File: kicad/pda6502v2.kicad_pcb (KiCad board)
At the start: 4 copper layers, 100 x 100 mm, 91 parts, among them J1 GPIO1, J2 GPIO2, J3 UART, J4 Screw_Terminal_01x02, J5 Conn_02x04_Odd_Even, J6 ICSP, J7 SPI, J8 FPGA_EXT, J9 SID, SW1 SW_Push, SW2 SW_Push, U1 W65C02SxP, U10 LT3030, U11 SC28L92A1B, U2 W65C22SxP, U3 W65C22SxP, U4 DS1818, U5 AS6C4008-55PCN, U6 ARMSID, U7 AT25M01, U8 ICE40HX4K-TQ144, U9 TLV1117-33, X1 8 MHz, X2 3.6864 MHz

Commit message: routing WIP: mostly ICSP to flash, a bit of BLINKEN
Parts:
- moved C10 25.2 mm to (132.9, 122.9)
- moved U7 19.3 mm to (131.6, 122.2)
- moved X1 5.36 mm to (132.1, 115.1)
- moved D11 5.06 mm to (102.9, 121.4), turned to 180 degrees
- moved U6 2.84 mm to (110.5, 90.2)
- moved C31 2.84 mm to (121.9, 102.9)
- moved C28 2.84 mm to (121.9, 100.3)
- moved C9 2.84 mm to (122.7, 90.2)
- moved J5 2.54 mm to (101.6, 110.5)
- moved SW2 2.54 mm to (101.6, 105.4)
- moved C2 1.27 mm to (154.9, 92.7)
- moved C6 1.27 mm to (174.0, 92.7)
- moved C1 1.27 mm to (135.9, 62.2)
- moved C4 1.27 mm to (124.5, 44.5)
- moved U1 1.27 mm to (132.1, 44.5)
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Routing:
- net /FLASH_~CS: track 0.00 -> 42.3 mm
- net /FLASH_SCK: track 0.00 -> 38.6 mm
- net /VCC_FLASH: track 0.00 -> 38.6 mm, vias 0 -> 3
- net /FLASH_MISO: track 0.00 -> 33.4 mm
- net /FLASH_MOSI: track 0.00 -> 31.5 mm
- net +2V5: track 125.9 -> 100.1 mm
- net /~RESET: track 21.5 -> 14.8 mm
- net +3V3: track 61.5 -> 68.2 mm
- net +5V: track 90.8 -> 84.6 mm
- net +1V2: track 97.1 -> 91.1 mm
- net GND: track 70.7 -> 65.7 mm, vias 21 -> 22
- net /UART_RXB~IRQ: track 14.0 -> 12.3 mm
- net /CLOCKSRC: track 7.79 -> 8.69 mm
- net Net-(U11-Pad30): track 20.9 -> 21.7 mm
- net /SPI_CLOCK: track 35.0 -> 34.3 mm
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
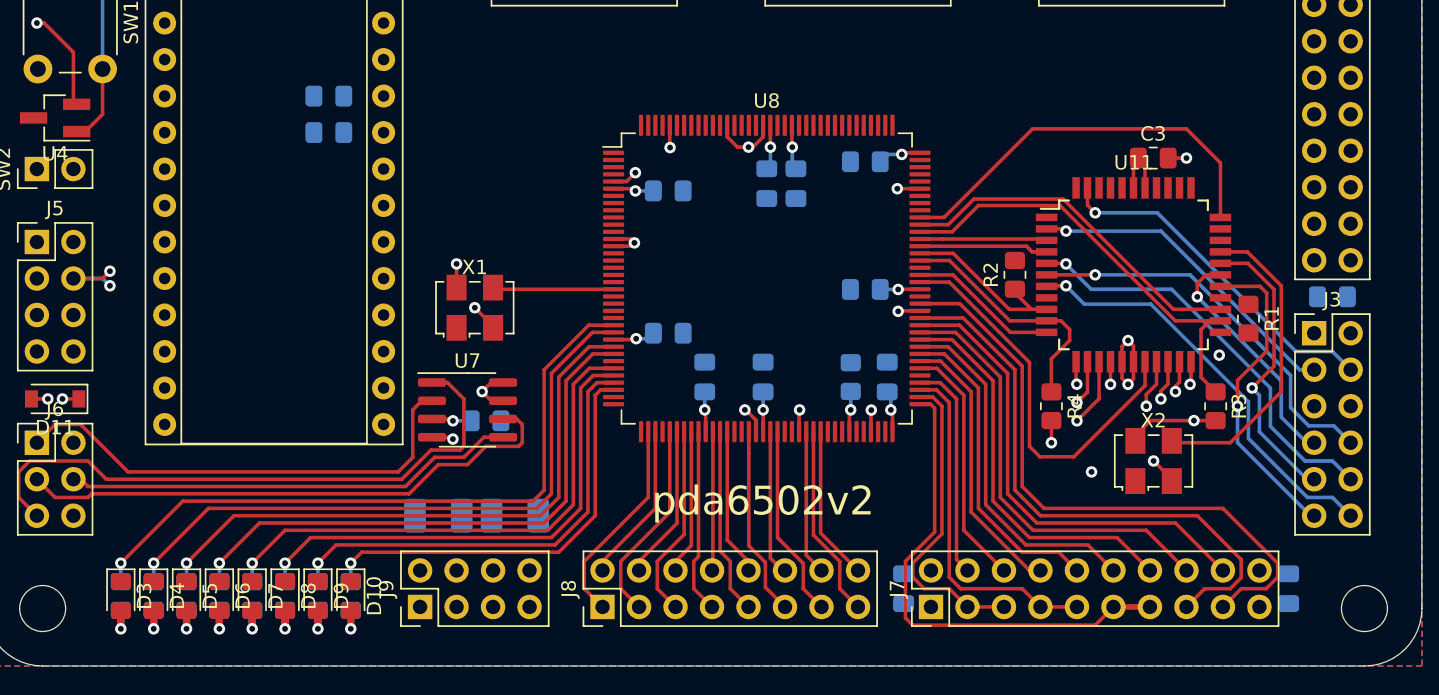
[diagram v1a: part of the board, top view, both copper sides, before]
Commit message: routing/placement; SID, FPGA, UART shifted away from centre.
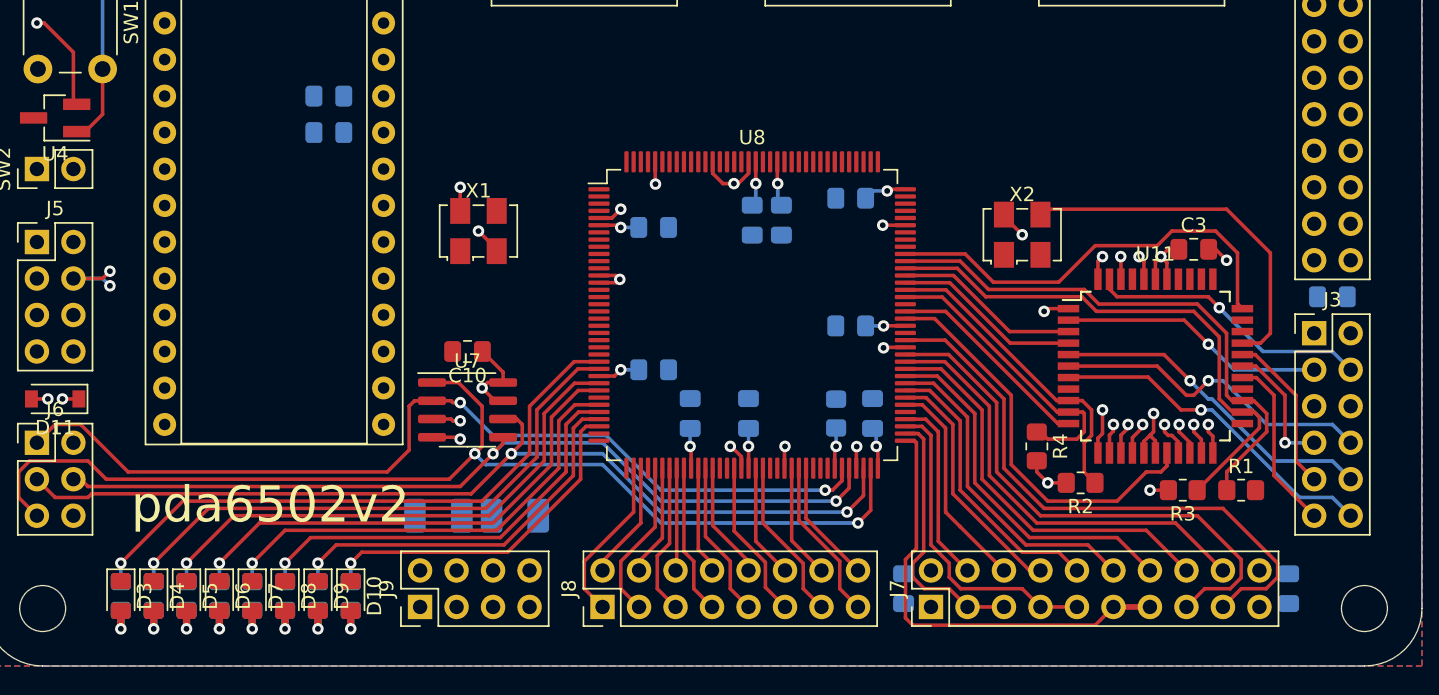
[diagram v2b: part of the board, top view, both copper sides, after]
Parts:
- C10: moved to F.Cu
- moved X2 18.2 mm to (170.2, 110.0)
- moved R2 15.2 mm to (174.2, 127.3), turned to 180 degrees
- moved R1 11.9 mm to (185.4, 127.8), turned to 0 degrees
- moved C3 6.95 mm to (182.1, 111.0)
- moved U11 6.53 mm to (179.5, 119.1)
- moved R3 6.27 mm to (181.4, 127.8), turned to 180 degrees
- moved X1 5.34 mm to (132.3, 109.7)
- moved C10 5.00 mm to (131.6, 118.1), turned to 180 degrees
- moved R4 2.97 mm to (171.2, 124.7)
- moved C22 2.74 mm to (144.5, 109.5)
- moved C14 2.74 mm to (158.2, 116.3)
- moved C17 2.74 mm to (159.8, 122.4)
- moved C23 2.74 mm to (151.4, 109.0)
- moved C24 2.74 mm to (158.2, 107.4)
- moved U8 2.74 mm to (151.4, 115.6)
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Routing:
- net /FLASH_~CS: track 42.3 -> 77.4 mm, vias 0 -> 2
- net +1V2: track 91.1 -> 124.8 mm
- net /FLASH_MISO: track 33.4 -> 65.5 mm, vias 0 -> 2
- net /FLASH_MOSI: track 31.5 -> 60.3 mm, vias 0 -> 2
- net /FLASH_SCK: track 38.6 -> 67.2 mm, vias 0 -> 2
- net +2V5: track 100.1 -> 125.9 mm
- net +5V: track 84.6 -> 99.0 mm
- net /UART_RXA~IRQ: track 24.8 -> 38.6 mm
- net /UARTA_RTS: track 22.4 -> 12.5 mm, vias 1 -> 0
- net /UART_RXB~IRQ: track 12.3 -> 22.0 mm
- net /UARTA_RX: track 20.4 -> 11.8 mm, vias 1 -> 0
- net /CLOCKSRC: track 8.69 -> 0.42 mm
- net /UART_TXA~IRQ: track 30.6 -> 37.6 mm
- net /UARTA_TX: track 16.6 -> 10.2 mm
- net /UARTB_RX: track 29.0 -> 23.2 mm
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
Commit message: more routing; SID connector, misc power etc.
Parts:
- moved C8 5.98 mm to (193.8, 81.3), turned to 0 degrees
- moved C7 2.03 mm to (189.7, 81.3)
- moved C5 0.82 mm to (190.8, 48.0), turned to 180 degrees
- moved C28 0.76 mm to (122.7, 100.3)
- moved C31 0.76 mm to (122.7, 102.9)
- moved C26 0.46 mm to (161.5, 134.9)
- moved C27 0.36 mm to (189.0, 134.4)
- turned C25 to 180 degrees
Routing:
- net +5V: track 99.0 -> 165.1 mm
- net /SID_X: track 0.00 -> 46.9 mm
- net /SID_Y: track 0.00 -> 42.8 mm
- net Net-(C29-Pad1): track 0.00 -> 42.4 mm
- net Net-(C30-Pad1): track 0.00 -> 40.4 mm
- net +3V3: track 67.0 -> 85.4 mm, vias 17 -> 20
- net +1V2: track 124.8 -> 132.4 mm, vias 4 -> 5
- net /SID_IN: track 0.00 -> 7.36 mm
- net GND: track 62.2 -> 69.2 mm, vias 18 -> 21
- net /SID_OUT: track 0.00 -> 3.96 mm
- net /VCC_FLASH: track 41.5 -> 44.9 mm

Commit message: Lots of routing. Nearly done, but getting tight.
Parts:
- removed the U3 at (170.2, 44.5)
- added U2: W65C22SxP, Package_DIP:DIP-40_W15.24mm, F.Cu at (151.1, 44.5)
- C28, C31: moved to F.Cu
- moved U3 19.1 mm to (170.2, 44.5)
- moved X2 9.56 mm to (179.3, 107.2)
- moved C10 7.89 mm to (129.5, 125.7)
- moved X1 7.27 mm to (135.4, 116.3)
- moved C31 6.60 mm to (129.3, 102.9), turned to 0 degrees
- moved C28 6.58 mm to (129.3, 100.3), turned to 0 degrees
- moved C29 6.48 mm to (136.0, 129.3), turned to 270 degrees
- moved C9 5.85 mm to (128.4, 91.4), turned to 270 degrees
- moved C2 4.88 mm to (151.1, 95.8), turned to 270 degrees
- moved C17 4.66 mm to (162.1, 126.5), turned to 0 degrees
- moved C15 4.26 mm to (145.8, 126.5), turned to 180 degrees
- moved C32 4.26 mm to (149.9, 126.5), turned to 180 degrees
- moved C22 4.20 mm to (140.7, 111.3), turned to 270 degrees
- moved R23 4.19 mm to (158.2, 126.5), turned to 0 degrees
- moved C30 2.30 mm to (132.6, 129.3), turned to 270 degrees
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- renumbered U2 to U3
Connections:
- J9 pad 3: /SID_X -> /SID_Y
- J9 pad 4: /SID_OUT -> /SID_X
- J9 pad 5: /SID_IN -> /SID_OUT
- J9 pad 6: /SID_Y -> /SID_IN
- U5 pad 10: /A2 -> /A5
- U5 pad 11: /A1 -> /A6
- U5 pad 12: /A0 -> /A7
- U5 pad 17: /D3 -> /D7
- U5 pad 18: /D4 -> /D6
- U5 pad 20: /D6 -> /D4
- U5 pad 21: /D7 -> /D3
- U5 pad 5: /A7 -> /A0
- U5 pad 6: /A6 -> /A1
- U5 pad 7: /A5 -> /A2
- U5 pad 8: /A4 -> /A3
- U5 pad 9: /A3 -> /A4
- U8 pad 12: Net-(U8-Pad12) -> /SID_~CS
- U8 pad 16: Net-(U8-Pad16) -> /RESET
- U8 pad 17: Net-(U8-Pad17) -> /~RESET
- U8 pad 22: /RESET -> Net-(U8-Pad22)
- U8 pad 23: /~RESET -> Net-(U8-Pad23)
- U8 pad 24: /SID_~CS -> Net-(U8-Pad24)
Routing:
- net /A3: track 1.78 -> 197.4 mm, vias 1 -> 7
- net /A2: track 1.70 -> 196.6 mm, vias 1 -> 7
- net /A1: track 1.58 -> 195.8 mm, vias 1 -> 7
- net /D0: track 2.12 -> 195.7 mm, vias 1 -> 5
- net /A0: track 1.71 -> 193.9 mm, vias 1 -> 7
- net /D1: track 3.13 -> 186.5 mm, vias 1 -> 5
- net /D2: track 2.21 -> 185.3 mm, vias 1 -> 5
- net /R~W: track 0.00 -> 164.6 mm, vias 0 -> 3
- net /D3: track 2.10 -> 166.1 mm, vias 1 -> 4
- net /D4: track 2.30 -> 164.0 mm, vias 1 -> 4
- net /D5: track 2.19 -> 154.1 mm, vias 1 -> 4
- net /D6: track 2.53 -> 151.3 mm, vias 1 -> 4
- net /D7: track 2.28 -> 142.1 mm, vias 1 -> 4
- net /CLOCK: track 0.00 -> 132.7 mm, vias 0 -> 3
- net /GPIO2A0: track 0.00 -> 94.5 mm, vias 0 -> 2
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
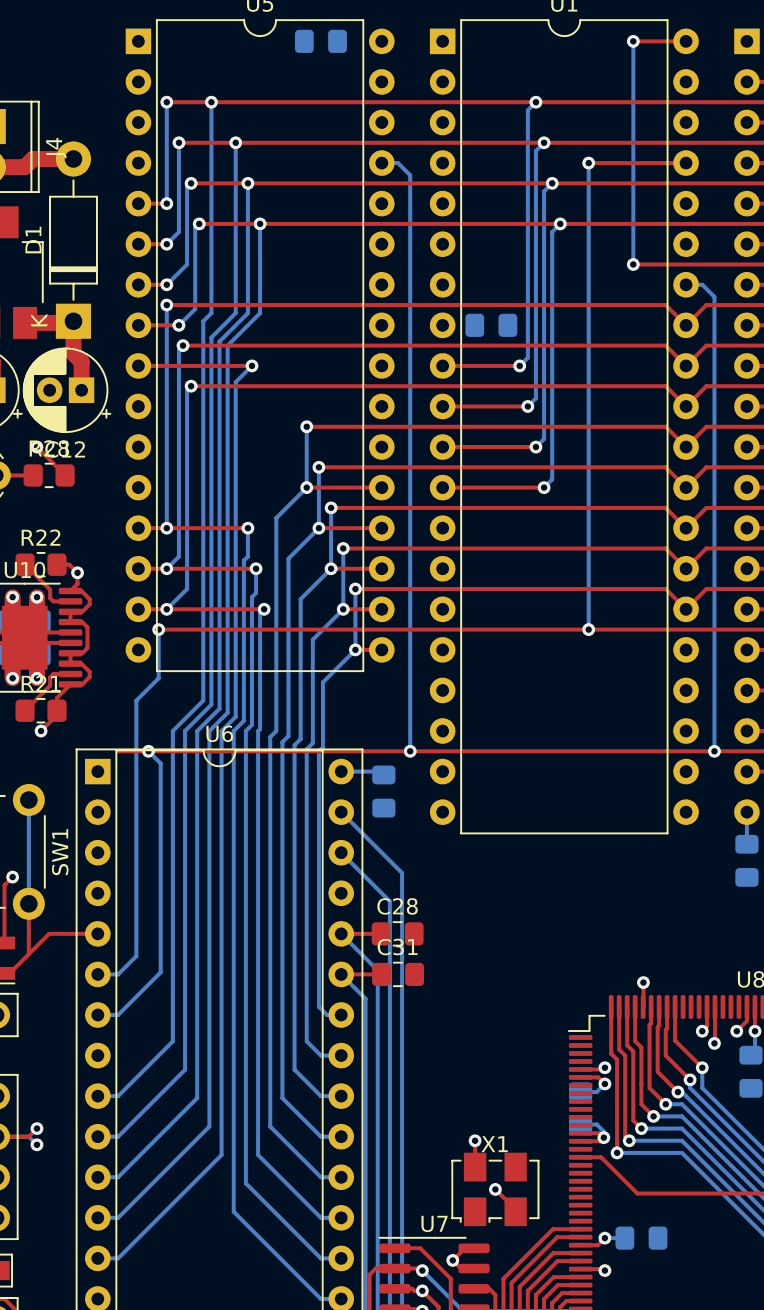
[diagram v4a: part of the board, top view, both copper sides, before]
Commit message: ARMSID routing improvements; fewer vias, straighter tracks.
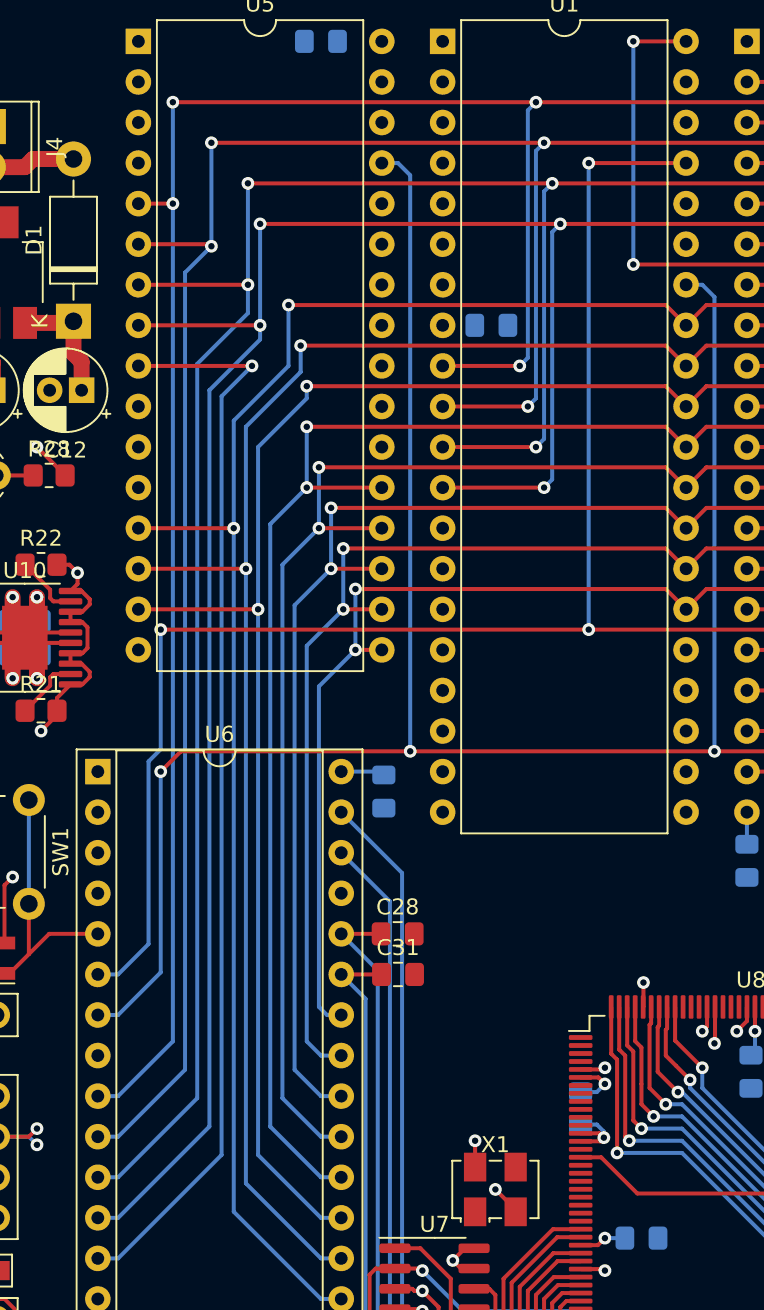
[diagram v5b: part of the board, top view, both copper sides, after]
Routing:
- net /D0: track 195.7 -> 188.3 mm, vias 5 -> 4
- net /A0: track 193.9 -> 186.5 mm, vias 7 -> 6
- net /D1: track 186.5 -> 179.3 mm, vias 5 -> 4
- net /D2: track 185.3 -> 178.2 mm, vias 5 -> 4
- net /A1: track 195.8 -> 189.3 mm, vias 7 -> 6
- net /A3: track 197.4 -> 191.8 mm, vias 7 -> 6
- net /A2: track 196.6 -> 191.1 mm, vias 7 -> 6
- net /R~W: track 164.6 -> 160.9 mm

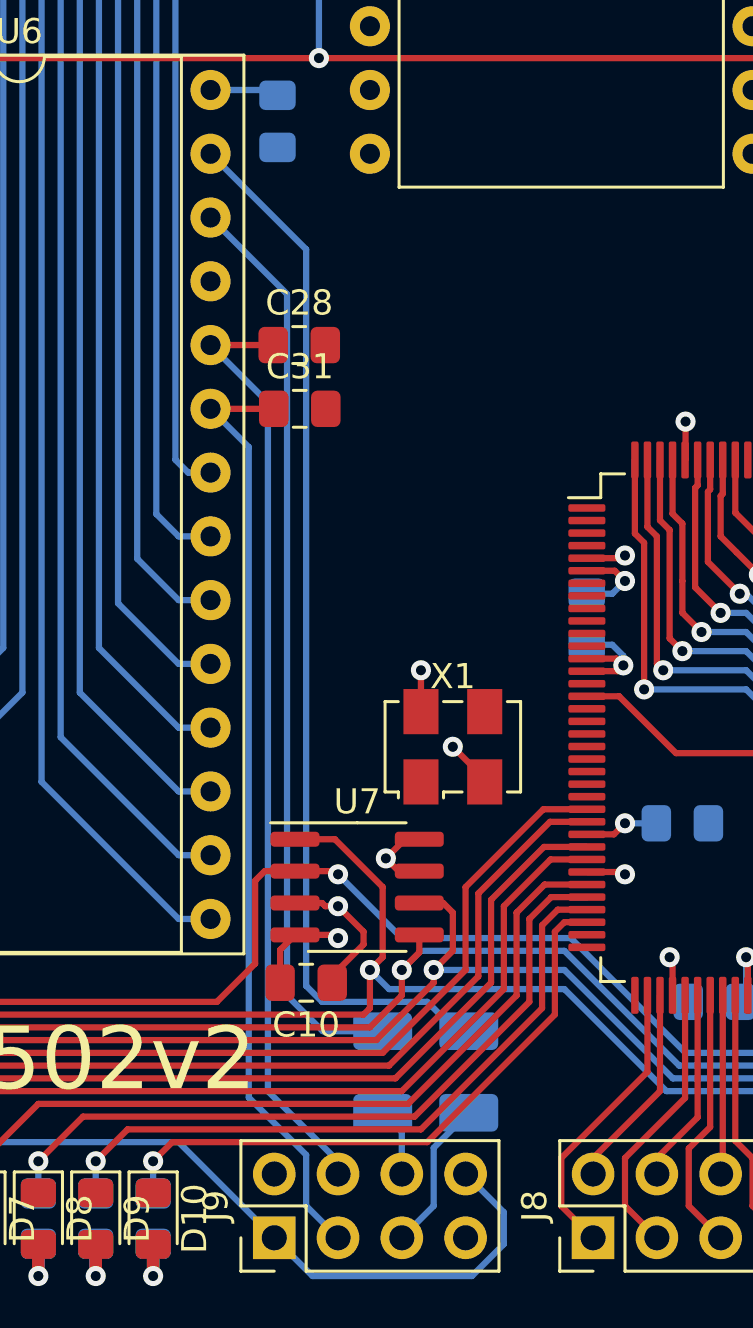
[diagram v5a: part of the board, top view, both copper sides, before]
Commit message: ARMSID X/Y caps moved from IC to headers; making room.
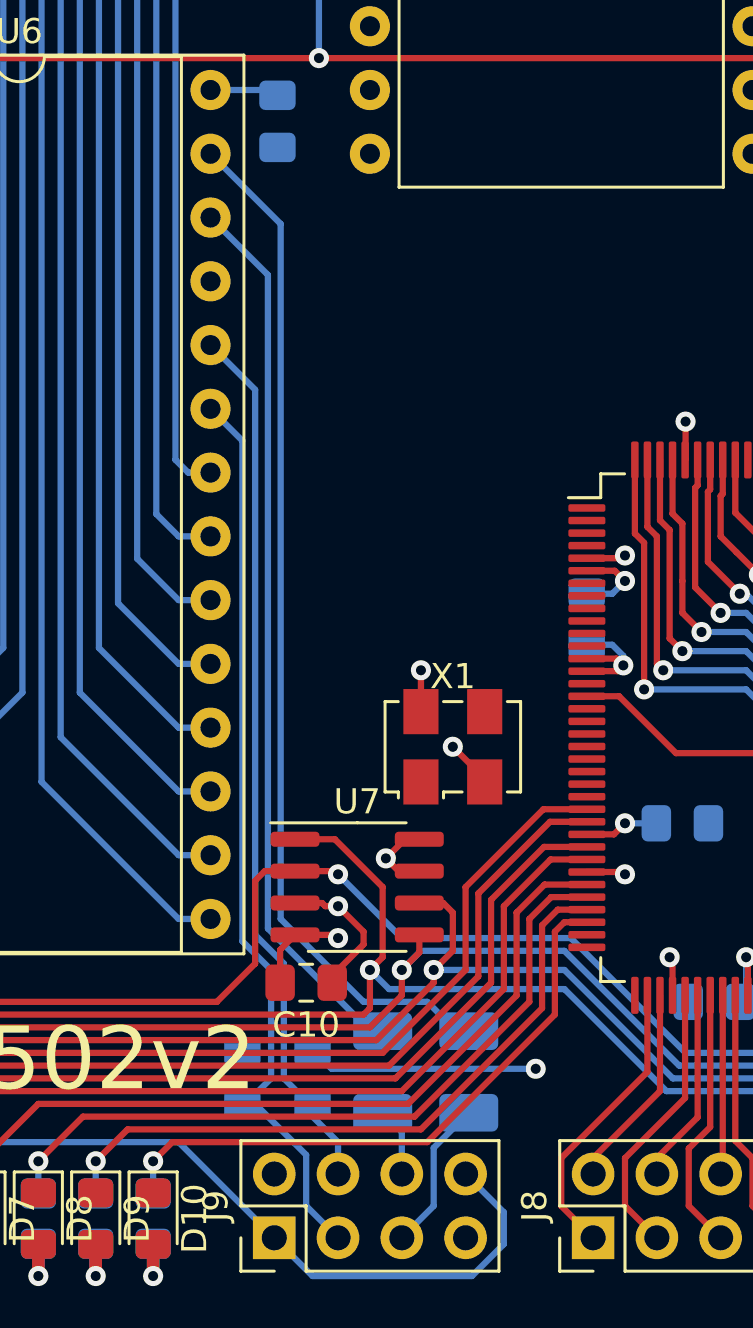
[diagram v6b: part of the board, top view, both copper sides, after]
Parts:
- C28, C31: moved to B.Cu
- moved C28 29.2 mm to (129.8, 129.5), turned to 90 degrees
- moved C31 26.8 mm to (127.0, 129.5), turned to 90 degrees
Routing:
- net GND: track 68.6 -> 77.7 mm, vias 21 -> 22
- net /SID_X: track 37.6 -> 35.2 mm
- net /SID_Y: track 37.6 -> 36.4 mm
- net Net-(C30-Pad1): track 36.6 -> 35.5 mm
- net Net-(C29-Pad1): track 41.9 -> 41.0 mm

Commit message: More routing, more stuck.
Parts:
- moved C1 4.95 mm to (130.2, 62.2), turned to 270 degrees
- moved C9 4.95 mm to (125.7, 87.2), turned to 90 degrees
- moved X1 1.40 mm to (134.0, 116.3)
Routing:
- net /~RESET: track 83.6 -> 227.1 mm, vias 3 -> 4
- net /~VECPULL: track 0.00 -> 69.6 mm, vias 0 -> 1
- net /READY: track 0.00 -> 68.5 mm, vias 0 -> 1
- net /~IRQ: track 0.00 -> 64.4 mm, vias 0 -> 1
- net /~MLOCK: track 0.00 -> 63.4 mm, vias 0 -> 1
- net /RAM_~CS: track 0.00 -> 62.9 mm, vias 0 -> 1
- net /~NMIRQ: track 0.00 -> 61.2 mm, vias 0 -> 1
- net /SYNC: track 0.00 -> 60.0 mm, vias 0 -> 1
- net /CLOCK: track 132.6 -> 175.4 mm, vias 3 -> 4
- net /SID_~CS: track 0.00 -> 33.1 mm
- net +1V2: track 165.0 -> 152.5 mm
- net /D3: track 166.1 -> 176.4 mm
- net /D4: track 164.0 -> 174.0 mm
- net /D5: track 154.1 -> 163.8 mm
- net /D0: track 188.3 -> 197.8 mm
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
